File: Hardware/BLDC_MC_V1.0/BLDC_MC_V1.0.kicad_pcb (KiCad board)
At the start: 8 copper layers, 120 x 55 mm, 229 parts, among them J1 Conn_01x01_Pin, J2 Conn_01x01_Pin, J3 USB_C_Receptacle_USB2.0_16P, J4 Conn_02x03_Counter_Clockwise, J5 S6B-PH-K-S_LF__SN_, J6 Conn_01x01_Pin, J7 Conn_01x01_Pin, J8 S10B-PHDSS LFSN, J9 Conn_01x01_Pin, Q1 BSC027N10NS5ATMA1, Q2 BSC027N10NS5ATMA1, Q3 BSC027N10NS5ATMA1, Q4 BSC027N10NS5ATMA1, Q5 BSC027N10NS5ATMA1, Q6 BSC027N10NS5ATMA1, Q7 BSC027N10NS5ATMA1, SW1 SW_Push, U1 LM76005RNPR, U10 TLV9061IDBVR, U11 TLV9061IDBVR, U12 TLV9061IDBVR, U13 TLV9061IDBVR, U14 TLV9061IDBVR, U15 TLV9061IDBVR, U16 LM74700QDRQ1, U2 TCAN334DR, U3 TLV9061IDBVR, U4 STM32G431RBT6, U5 LDL1117S33R, U6 DRV8353HRTAR, U7 NCV4274ADT50RKG, U8 25LC256-E_SN, U9 USBLC6-2SC6, Y1 7M-24.000MAAJ-T, Y2 ABS07-32.768KHZ-T

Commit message: Update the layout of the board
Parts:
- moved C60 16.9 mm to (91.7, 21.7)
- moved C63 16.9 mm to (87.3, 18.6)
- moved R52 16.9 mm to (91.7, 23.2)
- moved R50 16.9 mm to (91.7, 18.7)
- moved R51 16.9 mm to (91.7, 20.2)
- moved U11 16.9 mm to (87.2, 21.6)
- moved C17 16.2 mm to (87.0, 35.8)
- moved R45 16.2 mm to (91.5, 35.6)
- moved R46 16.2 mm to (91.5, 37.1)
- moved U3 16.2 mm to (87.0, 38.9)
- moved C58 16.2 mm to (91.5, 38.6)
- moved R15 16.2 mm to (91.5, 40.1)
- moved C65 2.99 mm to (150.4, 31.8), turned to 0 degrees
- moved C64 1.15 mm to (149.5, 22.7)
- moved C88 0.52 mm to (40.6, 39.9)
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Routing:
- net /BLDC_MC_V1.0_Connectors/Hall_A: track 0.00 -> 61.3 mm, vias 0 -> 1
- net /BLDC_MC_V1.0_Connectors/Hall_C: track 0.00 -> 60.9 mm, vias 0 -> 1
- net /BLDC_MC_V1.0_Connectors/Hall_B: track 0.00 -> 59.0 mm, vias 0 -> 1
- net GND: track 53.8 -> 61.3 mm, vias 0 -> 2
- added copper zone on B.Cu, net GND

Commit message: Update board placement
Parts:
- moved NT4 13.9 mm to (66.3, 48.6)
- moved R5 2.91 mm to (66.7, 60.6), turned to -90 degrees
- moved R3 0.45 mm to (64.6, 57.7), turned to 90 degrees
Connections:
- net Net-(C32-Pad1) renamed /BLDC_MC_V1.0_Power/Buck_SW
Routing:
- net GND: track 61.3 -> 75.0 mm, vias 2 -> 3
- net +12V: track 6.89 -> 20.3 mm
- net Vin: track 7.94 -> 15.6 mm
- net Net-(U1-BOOT): track 0.00 -> 3.46 mm
- net AGND: track 0.00 -> 2.41 mm
- net /BLDC_MC_V1.0_Power/Buck_SW: track 0.00 -> 2.00 mm
- net Net-(U1-SYNC/MODE): track 1.58 -> 2.48 mm
- added copper zone on B.Cu, net /BLDC_MC_V1.0_Power/Buck_SW

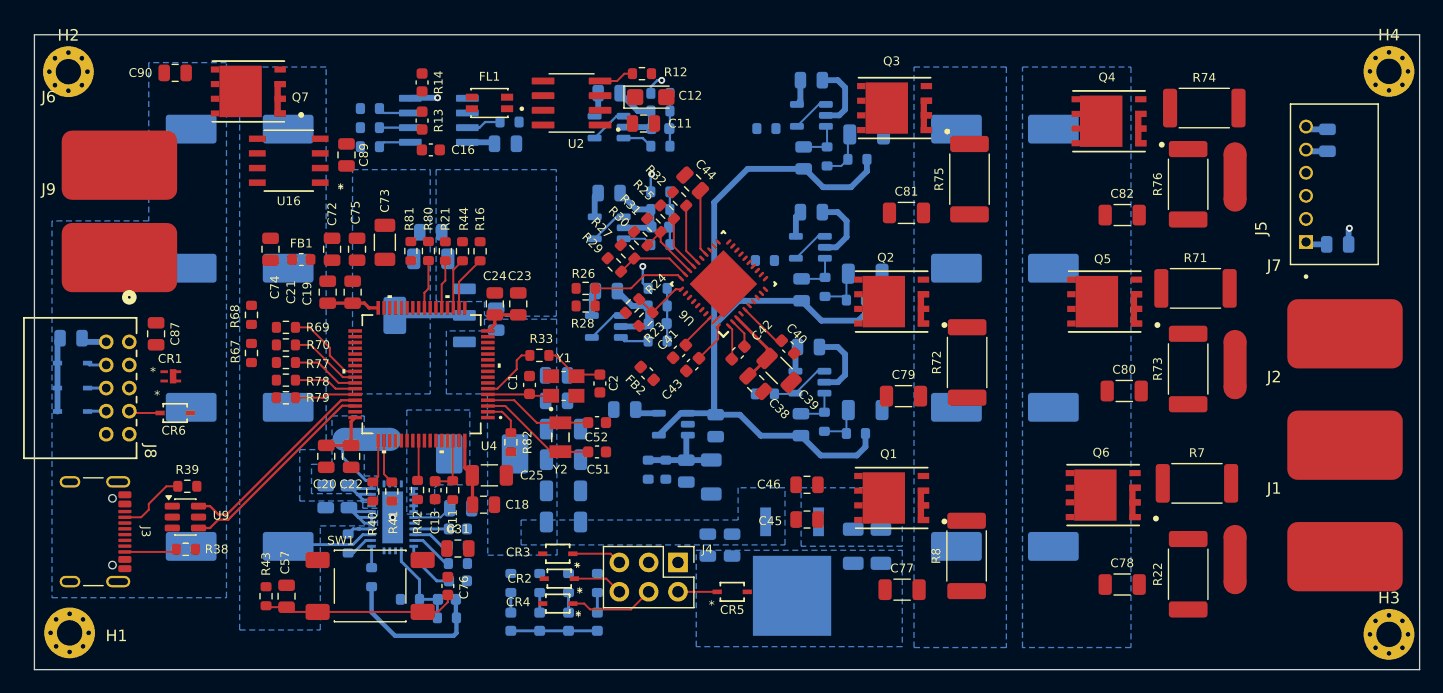
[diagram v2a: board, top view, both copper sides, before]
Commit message: Routing input voltage and add vias for power pads
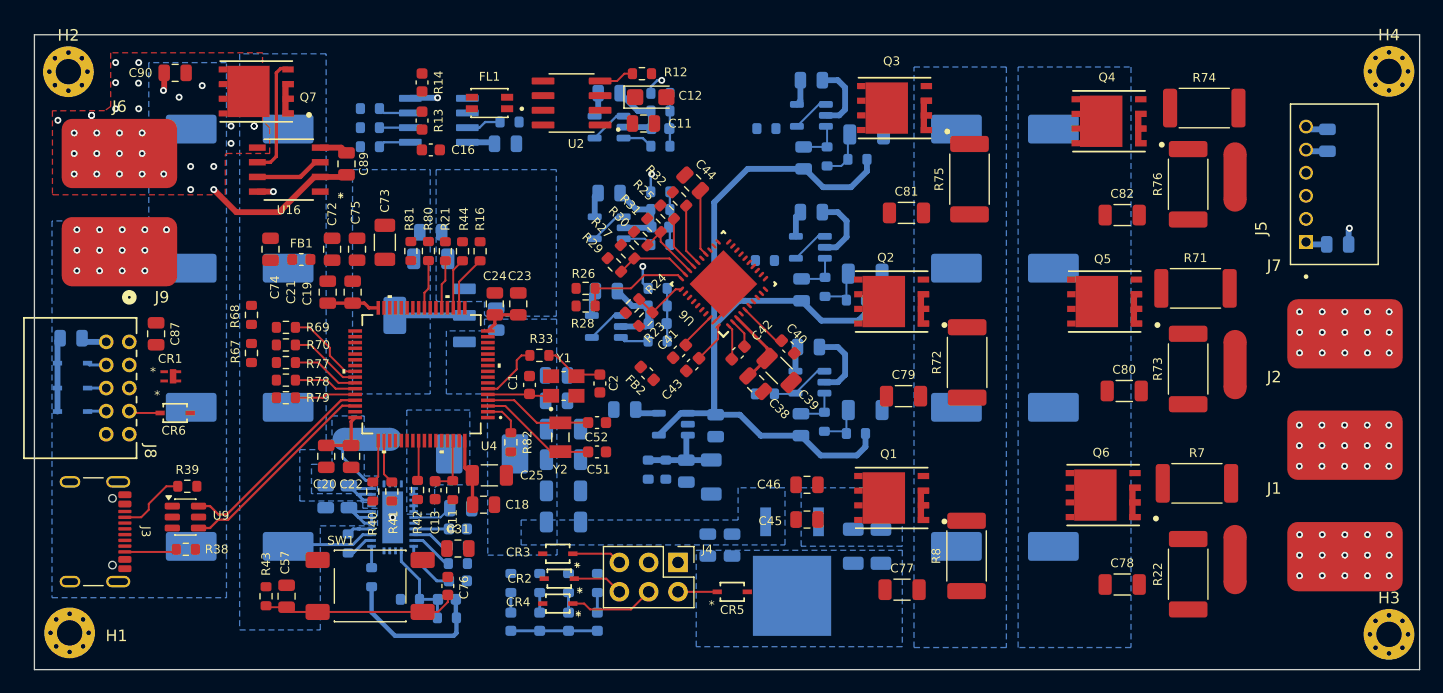
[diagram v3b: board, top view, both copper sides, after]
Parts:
- moved J6 1.02 mm to (44.8, 23.9)
- moved C89 0.77 mm to (64.5, 24.8)
- moved U16 0.77 mm to (59.5, 25.3)
- moved Q7 0.68 mm to (56.7, 18.5)
- moved J9 0.51 mm to (44.8, 32.4)
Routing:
- net /BLDC_MC_V1.0_Connectors/Vin_DC: track 0.00 -> 13.6 mm, vias 0 -> 32
- net Net-(U16-GATE): track 0.00 -> 10.3 mm
- net Net-(U16-N.C-Pad3): track 0.00 -> 5.97 mm
- net Net-(U16-VCAP): track 0.00 -> 2.46 mm
- net GND: track 75.0 -> 76.5 mm, vias 3 -> 17
- net Vin: track 15.6 -> 17.0 mm, vias 0 -> 1
- net /BLDC_MC_V1.0_3Phase_Inverter_legs/Phase_C: vias 0 -> 15
- net /BLDC_MC_V1.0_3Phase_Inverter_legs/Phase_B: vias 0 -> 15
- net /BLDC_MC_V1.0_3Phase_Inverter_legs/Phase_A: vias 0 -> 15
- added copper zone on F.Cu, net /BLDC_MC_V1.0_Connectors/Vin_DC
- added copper zone on In2.Cu, net /BLDC_MC_V1.0_Connectors/Vin_DC
- added copper zone on In3.Cu, net /BLDC_MC_V1.0_Connectors/Vin_DC
- added copper zone on In5.Cu, net /BLDC_MC_V1.0_Connectors/Vin_DC

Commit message: Update board layout
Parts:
- CR1: moved to B.Cu
- moved R39 3.74 mm to (47.2, 54.1), turned to 90 degrees
- moved R38 3.49 mm to (47.2, 59.2), turned to -90 degrees
- moved R27 1.88 mm to (87.5, 33.7)
- moved R29 1.43 mm to (88.7, 32.5)
- moved C16 1.29 mm to (73.1, 23.6)
- moved R14 1.28 mm to (72.3, 18.0)
- moved R13 1.25 mm to (72.3, 21.0)
- moved C31 0.40 mm to (74.2, 57.7)
- moved C87 0.30 mm to (48.0, 39.2)
- moved CR1 0.25 mm to (49.1, 43.0)
- moved CR2 0.13 mm to (82.8, 60.7)
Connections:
- net /BLDC_MC_V1.0_CAN_Transceiver/CANH renamed /BLDC_MC_V1.0_CAN_Transceiver/CAN_IC_P
- net /BLDC_MC_V1.0_CAN_Transceiver/CANL renamed /BLDC_MC_V1.0_CAN_Transceiver/CAN_IC_N
- net Net-(J3-D+-PadA6) renamed /BLDC_MC_V1.0_MCU/U_N
- net Net-(J3-D--PadA7) renamed /BLDC_MC_V1.0_MCU/U_P
- CR1 pad 1: /BLDC_MC_V1.0_CAN_Transceiver/CAN_H -> /BLDC_MC_V1.0_CAN_Transceiver/CAN_P
- CR1 pad 2: /BLDC_MC_V1.0_CAN_Transceiver/CAN_L -> /BLDC_MC_V1.0_CAN_Transceiver/CAN_N
- FL1 pad 3: /BLDC_MC_V1.0_CAN_Transceiver/CAN_L -> /BLDC_MC_V1.0_CAN_Transceiver/CAN_N
- FL1 pad 4: /BLDC_MC_V1.0_CAN_Transceiver/CAN_H -> /BLDC_MC_V1.0_CAN_Transceiver/CAN_P
- J8 pad 2: /BLDC_MC_V1.0_CAN_Transceiver/CAN_H -> /BLDC_MC_V1.0_CAN_Transceiver/CAN_N
- J8 pad 3: /BLDC_MC_V1.0_CAN_Transceiver/CAN_L -> /BLDC_MC_V1.0_CAN_Transceiver/CAN_P
- R13 pad 1: /BLDC_MC_V1.0_CAN_Transceiver/CAN_H -> /BLDC_MC_V1.0_CAN_Transceiver/CAN_P
- R14 pad 2: /BLDC_MC_V1.0_CAN_Transceiver/CAN_L -> /BLDC_MC_V1.0_CAN_Transceiver/CAN_N
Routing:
- net GND: track 76.5 -> 146.4 mm, vias 17 -> 29
- net /BLDC_MC_V1.0_CAN_Transceiver/CAN_N: track 0.00 -> 45.7 mm
- net /BLDC_MC_V1.0_CAN_Transceiver/CAN_P: track 0.00 -> 45.5 mm
- net /BLDC_MC_V1.0_Connectors/UART4_RX: track 1.73 -> 31.8 mm, vias 0 -> 1
- net +3.3V: track 50.1 -> 80.2 mm, vias 0 -> 12
- net Vin: track 17.0 -> 46.9 mm
- net /BLDC_MC_V1.0_Connectors/UART4_TX: track 1.79 -> 30.1 mm, vias 0 -> 1
- net /BLDC_MC_V1.0_MCU/MISO: track 0.00 -> 22.7 mm, vias 0 -> 2
- net GNDA: track 0.00 -> 18.1 mm
- net /BLDC_MC_V1.0_Connectors/I2C3_SDA: track 1.85 -> 19.9 mm
- net /BLDC_MC_V1.0_Memory/SI: track 0.00 -> 16.3 mm, vias 0 -> 2
- net /BLDC_MC_V1.0_Memory/CS: track 2.83 -> 18.7 mm, vias 0 -> 1
- net /BLDC_MC_V1.0_Memory/SCK_M: track 0.00 -> 14.9 mm, vias 0 -> 2
- net /BLDC_MC_V1.0_Connectors/I2C3_SCL: track 2.73 -> 17.2 mm
- net +12V: track 20.3 -> 32.6 mm
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- added copper zone on In3.Cu, net +3.3V
- added copper zone on F.Cu, net GND
- added copper zone on F.Cu, net Vref

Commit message: Update board layout
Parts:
- moved CR1 1.10 mm to (48.0, 43.1)
- moved C31 1.01 mm to (74.6, 58.6)
- moved C13 0.95 mm to (72.2, 52.1)
- moved R11 0.95 mm to (73.7, 52.1)
- moved R40 0.95 mm to (66.8, 52.2)
- moved R41 0.95 mm to (68.4, 52.2)
- moved R42 0.95 mm to (70.7, 52.1)
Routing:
- net Vin: track 46.9 -> 17.0 mm
- net GND: track 146.4 -> 170.7 mm, vias 29 -> 37
- net Net-(J4-Pin_6): track 4.50 -> 27.5 mm
- net +3.3V: track 80.2 -> 98.4 mm, vias 12 -> 20
- net Net-(J4-Pin_5): track 4.34 -> 22.3 mm
- net +12V: track 32.6 -> 41.6 mm
- net AGND: track 10.9 -> 17.2 mm, vias 0 -> 4
- net /BLDC_MC_V1.0_Connectors/UART4_RX: track 31.8 -> 34.3 mm
- net /BLDC_MC_V1.0_CAN_Transceiver/CAN_N: track 45.7 -> 48.1 mm
- net /BLDC_MC_V1.0_CAN_Transceiver/CAN_P: track 45.5 -> 47.7 mm
- net Net-(U14-IN-): track 3.30 -> 5.23 mm
- net Net-(U15-IN-): track 3.30 -> 5.19 mm
- net Net-(U1-BIAS): track 3.41 -> 5.22 mm, vias 0 -> 1
- net /BLDC_MC_V1.0_CAN_Transceiver/IC_TXD: track 6.01 -> 7.62 mm
- net /BLDC_MC_V1.0_Memory/SI: track 16.3 -> 17.4 mm
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- added copper zone on In5.Cu, net AGND

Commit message: Update board Placement
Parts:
- moved R17 2.34 mm to (68.7, 19.2)
- moved R18 2.34 mm to (80.8, 20.3)
- moved R19 2.34 mm to (68.7, 22.5)
- moved R20 2.34 mm to (68.7, 20.8)
- moved U8 2.34 mm to (74.7, 20.2)
- moved C61 2.34 mm to (80.5, 22.2)
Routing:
- net +3.3V: track 98.4 -> 155.6 mm, vias 20 -> 23
- net /BLDC_MC_V1.0_CAN_Transceiver/IC_TXD: track 7.62 -> 54.4 mm
- net /BLDC_MC_V1.0_CAN_Transceiver/RXD: track 6.98 -> 47.2 mm
- net /BLDC_MC_V1.0_CAN_Transceiver/CAN_SHDN: track 0.00 -> 39.1 mm, vias 0 -> 2
- net /BLDC_MC_V1.0_CAN_Transceiver/CAN_STB: track 0.00 -> 32.9 mm, vias 0 -> 2
- net GND: track 170.7 -> 189.0 mm, vias 37 -> 41
- net /BLDC_MC_V1.0_Memory/SCK_M: track 14.9 -> 17.4 mm
- net /BLDC_MC_V1.0_Connectors/UART4_RX: track 34.3 -> 31.9 mm
- net /BLDC_MC_V1.0_Memory/SI: track 17.4 -> 19.6 mm
- net /BLDC_MC_V1.0_MCU/MISO: track 23.4 -> 21.3 mm
- net Vin: vias 1 -> 10
- added copper zone on B.Cu, net AGND
- added copper zone on F.Cu, net Vin
- added copper zone on In2.Cu, net Vin
- added copper zone on In5.Cu, net Vin
